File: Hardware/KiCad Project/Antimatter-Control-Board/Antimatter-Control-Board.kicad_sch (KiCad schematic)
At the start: 6 parts, among them J1 3P JST XH, SW1 SW_SPST, U1 STM32C011F6Ux, U2 AP2210N-3.3TRG1

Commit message: Copy transceiver circuit from datasheet
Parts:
- C1, C2: value C -> 10u
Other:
- added sheet Transceiver (Transceiver.kicad_sch)
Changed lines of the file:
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@@
 			)
 		)
-		(property "Value" "C"
+		(property "Value" "10u"
 			(at 93.98 92.7099 0)
 			(effects
@@
 			)
 		)
-		(property "Value" "C"
+		(property "Value" "10u"
 			(at 82.55 102.8699 0)
 			(effects
@@
 				)
 			)
+		)
+	)
+	(sheet
+		(at 218.694 32.004)
+		(size 41.402 38.354)
+		(exclude_from_sim no)
+		(in_bom yes)
+		(on_board yes)
+		(dnp no)
+		(fields_autoplaced yes)
+		(stroke
+			(width 0.1524)
+			(type solid)
+		)
+		(fill
+			(color 0 0 0 0.0000)
+		)
+		(property "Sheetname" "Transceiver"
+			(at 218.694 31.2924 0)
+			(effects
+				(font
+					(size 1.27 1.27)
+				)
+				(justify left bottom)
+			)
+		)
+		(property "Sheetfile" "Transceiver.kicad_sch"
+			(at 218.694 70.9426 0)
+			(effects
+				(font
+					(size 1.27 1.27)
+				)
+				(justify left top)
+			)
+		)
+		(instances
+			(project "Antimatter-Control-Board"
+				(path "/ab2a7697-0e5e-4b53-bb59-6796636b3acd"
+					(page "2")
+				)
+			)

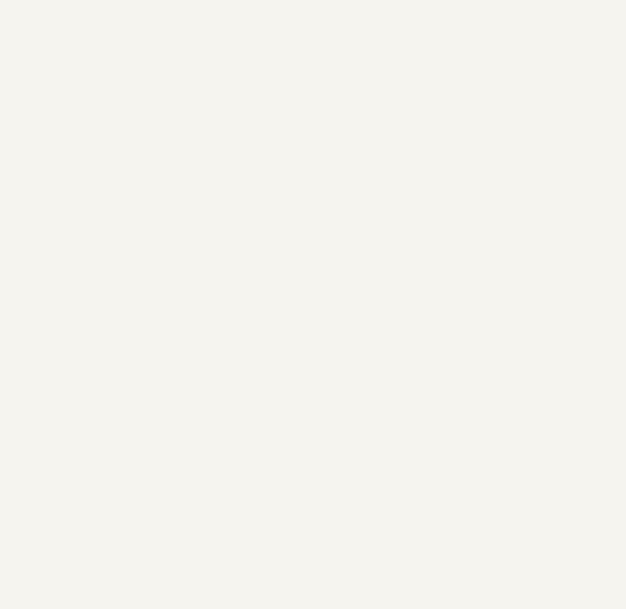
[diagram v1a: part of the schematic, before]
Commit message: Add motor driver
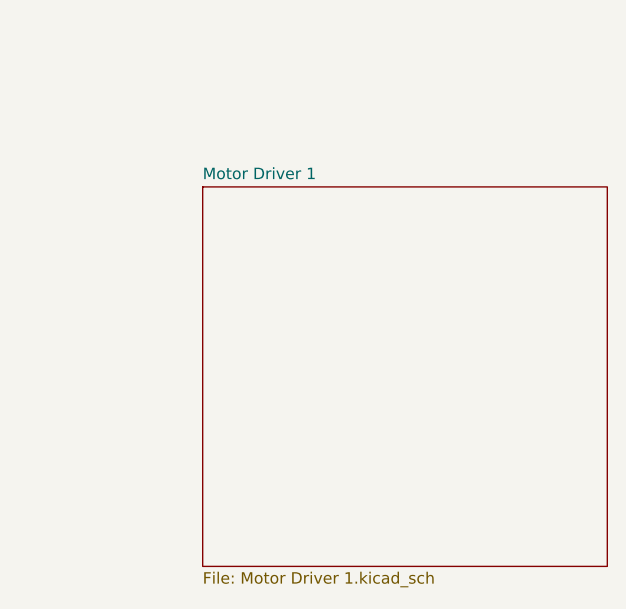
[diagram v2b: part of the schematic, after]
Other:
- added sheet Motor Driver 1 (Motor Driver 1.kicad_sch)
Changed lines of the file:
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@@
+		)
+	)
+	(sheet
+		(at 217.17 104.648)
+		(size 44.958 42.164)
+		(exclude_from_sim no)
+		(in_bom yes)
+		(on_board yes)
+		(dnp no)
+		(fields_autoplaced yes)
+		(stroke
+			(width 0.1524)
+			(type solid)
+		)
+		(fill
+			(color 0 0 0 0.0000)
+		)
+		(property "Sheetname" "Motor Driver 1"
+			(at 217.17 103.9364 0)
+			(effects
+				(font
+					(size 1.27 1.27)
+				)
+				(justify left bottom)
+			)
+		)
+		(property "Sheetfile" "Motor Driver 1.kicad_sch"
+			(at 217.17 147.3966 0)
+			(effects
+				(font
+					(size 1.27 1.27)
+				)
+				(justify left top)
+			)
+		)
+		(instances
+			(project "Antimatter-Control-Board"
+				(path "/ab2a7697-0e5e-4b53-bb59-6796636b3acd"
+					(page "3")
+				)
+			)
 		)
 	)

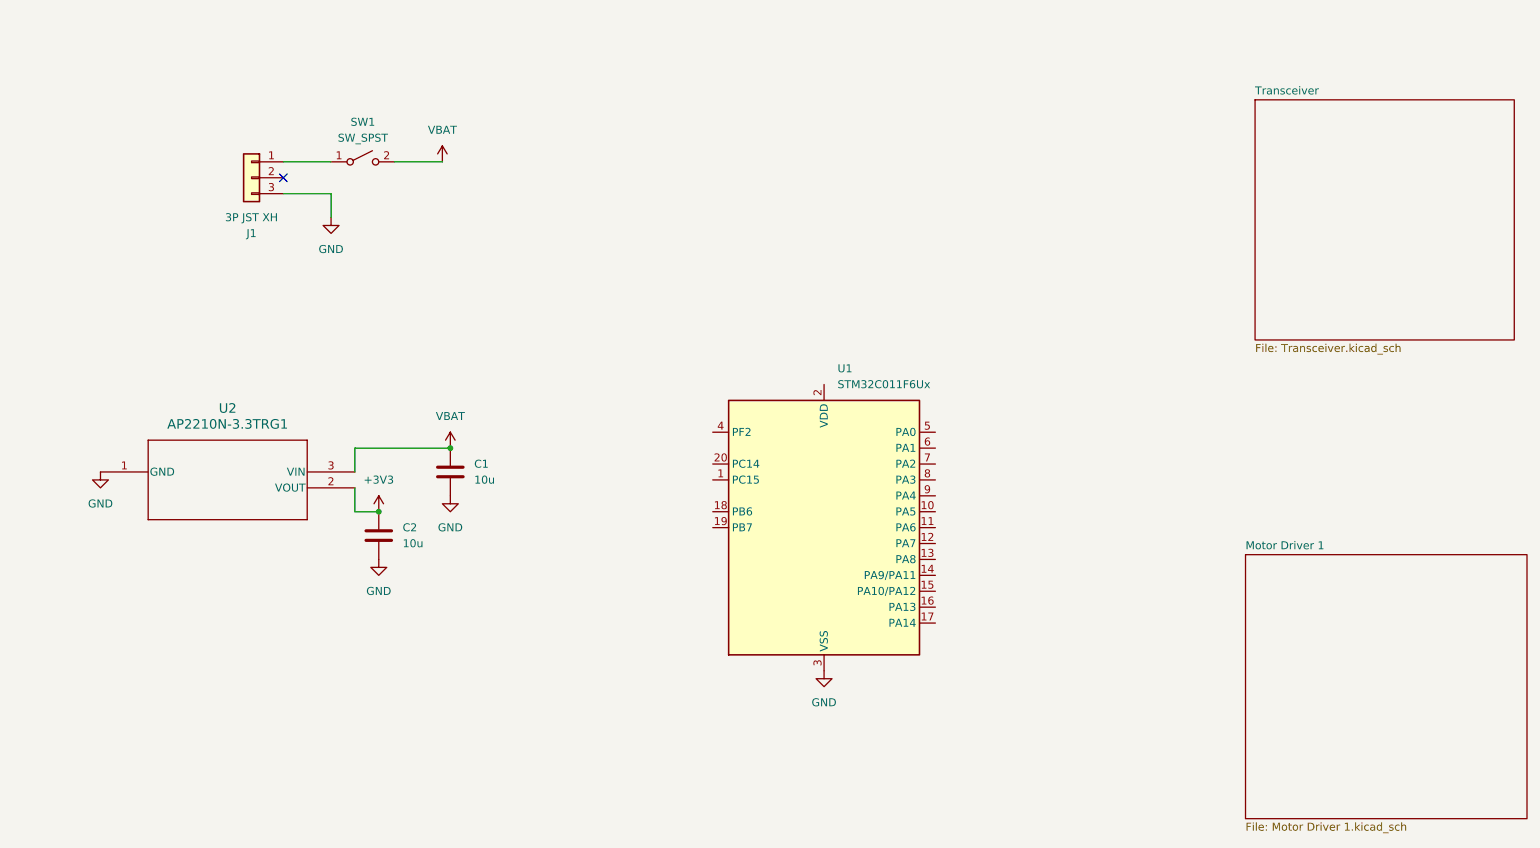
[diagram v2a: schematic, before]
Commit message: Add IMU and mag schematics
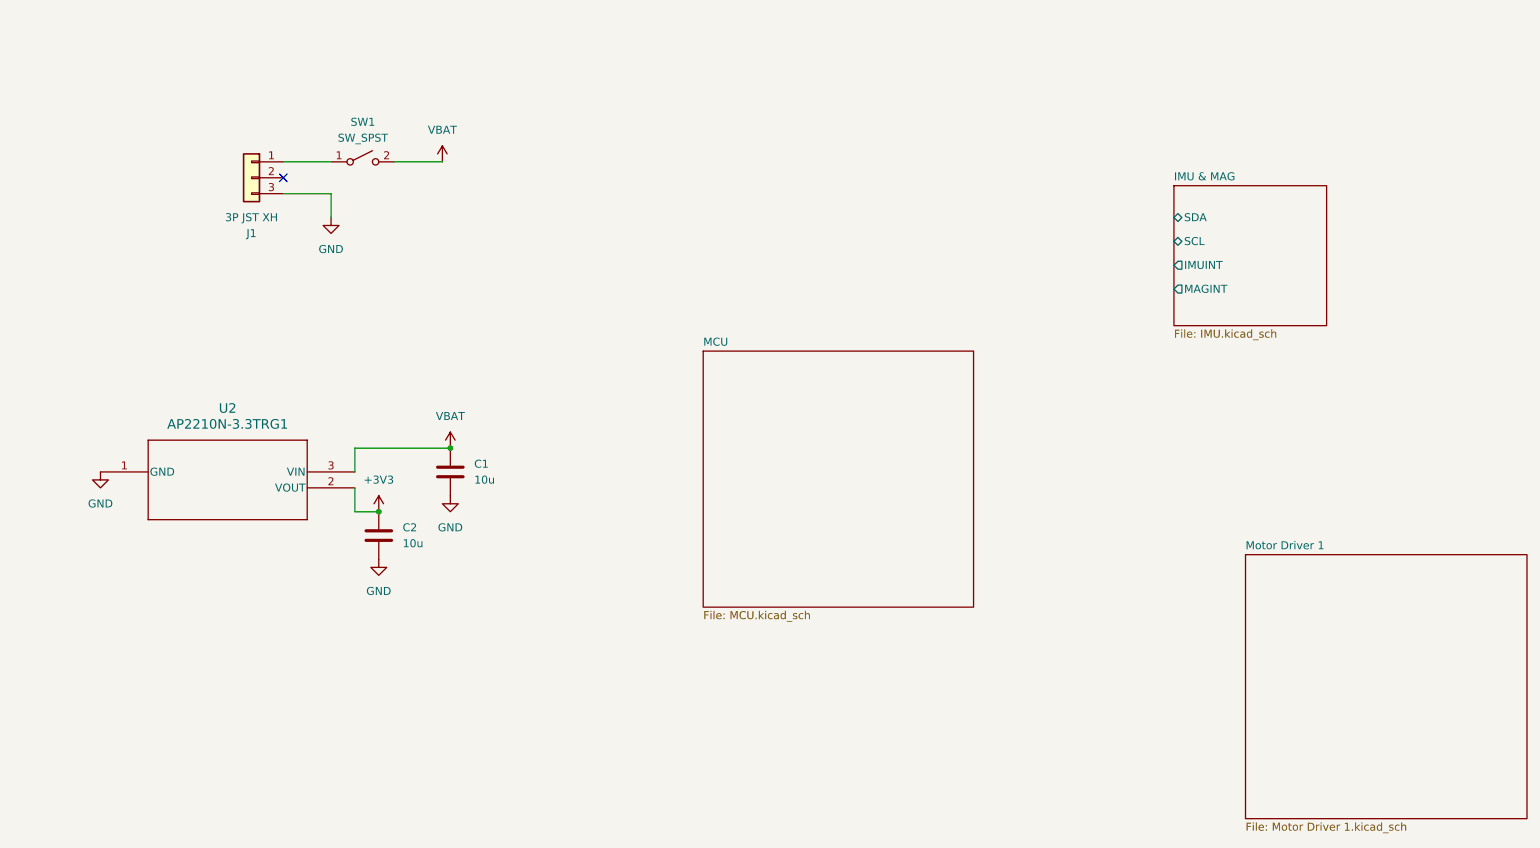
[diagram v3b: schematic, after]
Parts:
- removed U1: STM32C011F6Ux, Package_DFN_QFN:ST_UFQFPN-20_3x3mm_P0.5mm, symbol MCU_ST_STM32C0:STM32C011F6Ux
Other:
- removed sheet Transceiver
- added sheet IMU & MAG (IMU.kicad_sch)
- added sheet MCU (MCU.kicad_sch)
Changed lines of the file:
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@@
-	(symbol
-		(lib_id "power:GND")
-		(at 149.86 123.19 0)
-		(unit 1)
-		(exclude_from_sim no)
-		(in_bom yes)
-		(on_board yes)
-		(dnp no)
-		(fields_autoplaced yes)
-		(property "Reference" "#PWR01"
-			(at 149.86 129.54 0)
-			(effects
-				(font
-					(size 1.27 1.27)
-				)
-				(hide yes)
-			)
-		)
-		(property "Value" "GND"
-			(at 149.86 128.27 0)
-			(effects
-				(font
-					(size 1.27 1.27)
-				)
-			)
-		)
-		(property "Footprint" ""
-			(at 149.86 123.19 0)
-			(effects
-				(font
-					(size 1.27 1.27)
-				)
-				(hide yes)
-			)
-		)
-		(property "Datasheet" ""
-			(at 149.86 123.19 0)
-			(effects
-				(font
-					(size 1.27 1.27)
-				)
-				(hide yes)
-			)
-		)
-		(property "Description" "Power symbol creates a global label with name \"GND\" , ground"
-			(at 149.86 123.19 0)
-			(effects
-				(font
-					(size 1.27 1.27)
-				)
-				(hide yes)
-			)
-		)
-		(pin "1"
-		)
-		(instances
-			(project ""
-				(path "/ab2a7697-0e5e-4b53-bb59-6796636b3acd"
-					(reference "#PWR01")
-					(unit 1)
-				)
-			)
-		)
-	)
-	(symbol
-		(lib_id "MCU_ST_STM32C0:STM32C011F6Ux")
-		(at 149.86 100.33 0)
-		(unit 1)
-		(exclude_from_sim no)
-		(in_bom yes)
-		(on_board yes)
-		(dnp no)
-		(fields_autoplaced yes)
-		(property "Reference" "U1"
-			(at 152.0033 74.93 0)
-			(effects
-				(font
-					(size 1.27 1.27)
-				)
-				(justify left)
-			)
-		)
-		(property "Value" "STM32C011F6Ux"
-			(at 152.0033 77.47 0)
-			(effects
-				(font
-					(size 1.27 1.27)
-				)
-				(justify left)
-			)
-		)
-		(property "Footprint" "Package_DFN_QFN:ST_UFQFPN-20_3x3mm_P0.5mm"
-			(at 134.62 120.65 0)
-			(effects
-				(font
-					(size 1.27 1.27)
-				)
-				(justify right)
-				(hide yes)
-			)
-		)
-		(property "Datasheet" "https://www.st.com/resource/en/datasheet/stm32c011f6.pdf"
-			(at 149.86 100.33 0)
-			(effects
-				(font
-					(size 1.27 1.27)
-				)
-				(hide yes)
-			)
-		)
-		(property "Description" "STMicroelectronics Arm Cortex-M0+ MCU, 32KB flash, 6KB RAM, 48 MHz, 2.0-3.6V, 18 GPIO, UFQFPN20"
-			(at 149.86 100.33 0)
-			(effects
-				(font
-					(size 1.27 1.27)
-				)
-				(hide yes)
-			)
-		)
-		(pin "3"
-		)
-		(pin "4"
-		)
-		(pin "2"
-		)
-		(pin "18"
-		)
-		(pin "5"
-		)
-		(pin "13"
-		)
-		(pin "15"
-		)
-		(pin "11"
-		)
-		(pin "10"
-		)
-		(pin "17"
-		)
-		(pin "19"
-		)
-		(pin "16"
-		)
-		(pin "20"
-		)
-		(pin "7"
-		)
-		(pin "1"
-		)
-		(pin "9"
-		)
-		(pin "6"
-		)
-		(pin "12"
-		)
-		(pin "14"
-		)
-		(pin "8"
-		)
-		(instances
-			(project ""
-				(path "/ab2a7697-0e5e-4b53-bb59-6796636b3acd"
-					(reference "U1")
-					(unit 1)
-				)
-			)
-		)
-	)
 	(symbol
 		(lib_id "power:GND")
@@
 	)
 	(sheet
-		(at 218.694 32.004)
-		(size 41.402 38.354)
+		(at 205.74 45.72)
+		(size 24.384 22.352)
 		(exclude_from_sim no)
 		(in_bom yes)
@@
 			(color 0 0 0 0.0000)
 		)
-		(property "Sheetname" "Transceiver"
-			(at 218.694 31.2924 0)
+		(property "Sheetname" "IMU & MAG"
+			(at 205.74 45.0084 0)
 			(effects
 				(font
@@
 			)
 		)
-		(property "Sheetfile" "Transceiver.kicad_sch"
-			(at 218.694 70.9426 0)
+		(property "Sheetfile" "IMU.kicad_sch"
+			(at 205.74 68.6566 0)
 			(effects
 				(font
@@
 			)
 		)
+		(pin "MAGINT" output
+			(at 205.74 62.23 180)
+			(effects
+				(font
+					(size 1.27 1.27)
+				)
+				(justify left)
+			)
+		)
+		(pin "IMUINT" output
+			(at 205.74 58.42 180)
+			(effects
+				(font
+					(size 1.27 1.27)
+				)
+				(justify left)
+			)
+		)
+		(pin "SDA" bidirectional
+			(at 205.74 50.8 180)
+			(effects
+				(font
+					(size 1.27 1.27)
+				)
+				(justify left)
+			)
+		)
+		(pin "SCL" bidirectional
+			(at 205.74 54.61 180)
+			(effects
+				(font
+					(size 1.27 1.27)
+				)
+				(justify left)
+			)
+		)
 		(instances
 			(project "Antimatter-Control-Board"
 				(path "/ab2a7697-0e5e-4b53-bb59-6796636b3acd"
-					(page "2")
-				)
-			)
+					(page "4")
+				)
+			)
+		)
+	)
+	(sheet
+		(at 130.556 72.136)
+		(size 43.18 40.894)
+		(exclude_from_sim no)
+		(in_bom yes)
+		(on_board yes)
+		(dnp no)
+		(fields_autoplaced yes)
+		(stroke
+			(width 0.1524)
+			(type solid)
+		)
+		(fill
+			(color 0 0 0 0.0000)
+		)
+		(property "Sheetname" "MCU"
+			(at 130.556 71.4244 0)
+			(effects
+				(font
+					(size 1.27 1.27)
+				)
+				(justify left bottom)
+			)
+		)
+		(property "Sheetfile" "MCU.kicad_sch"
+			(at 130.556 113.6146 0)
+			(effects
+				(font
+					(size 1.27 1.27)
+				)
+				(justify left top)
+			)
+		)
+		(instances
+			(project "Antimatter-Control-Board"
+				(path "/ab2a7697-0e5e-4b53-bb59-6796636b3acd"
+					(page "3")
+				)
+			)

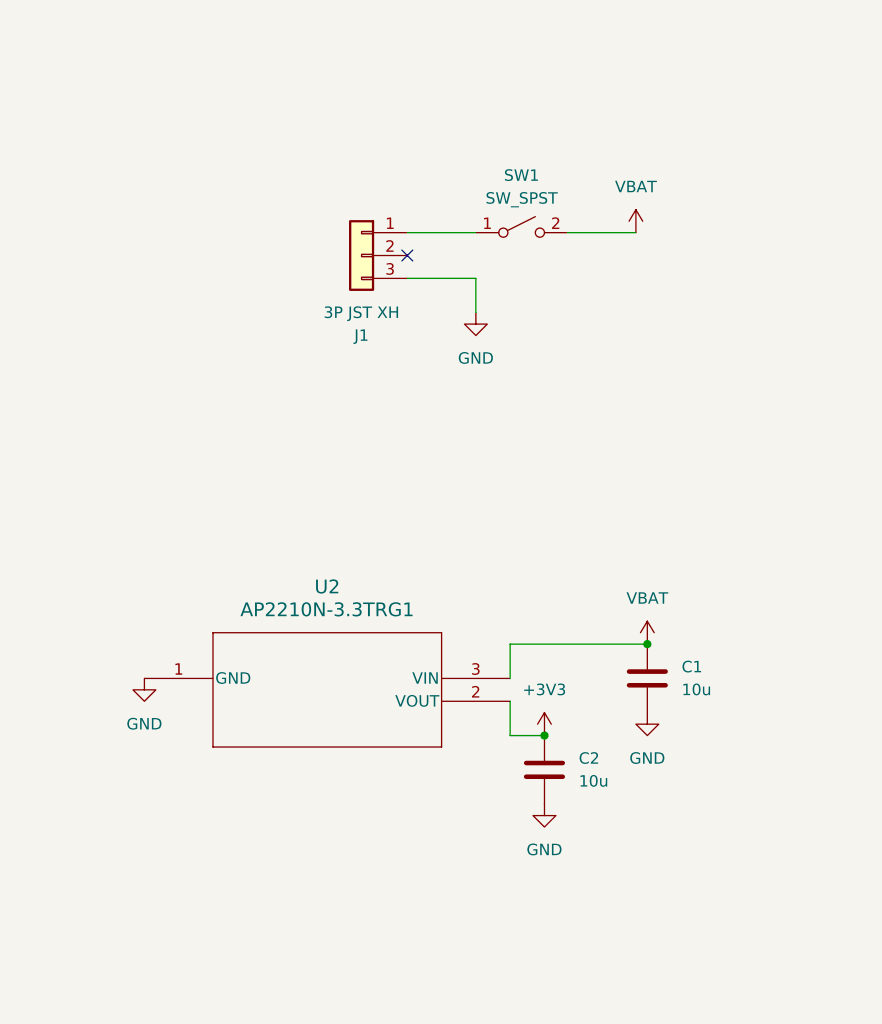
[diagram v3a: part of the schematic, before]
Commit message: Add power sheet and fix some ERC issues
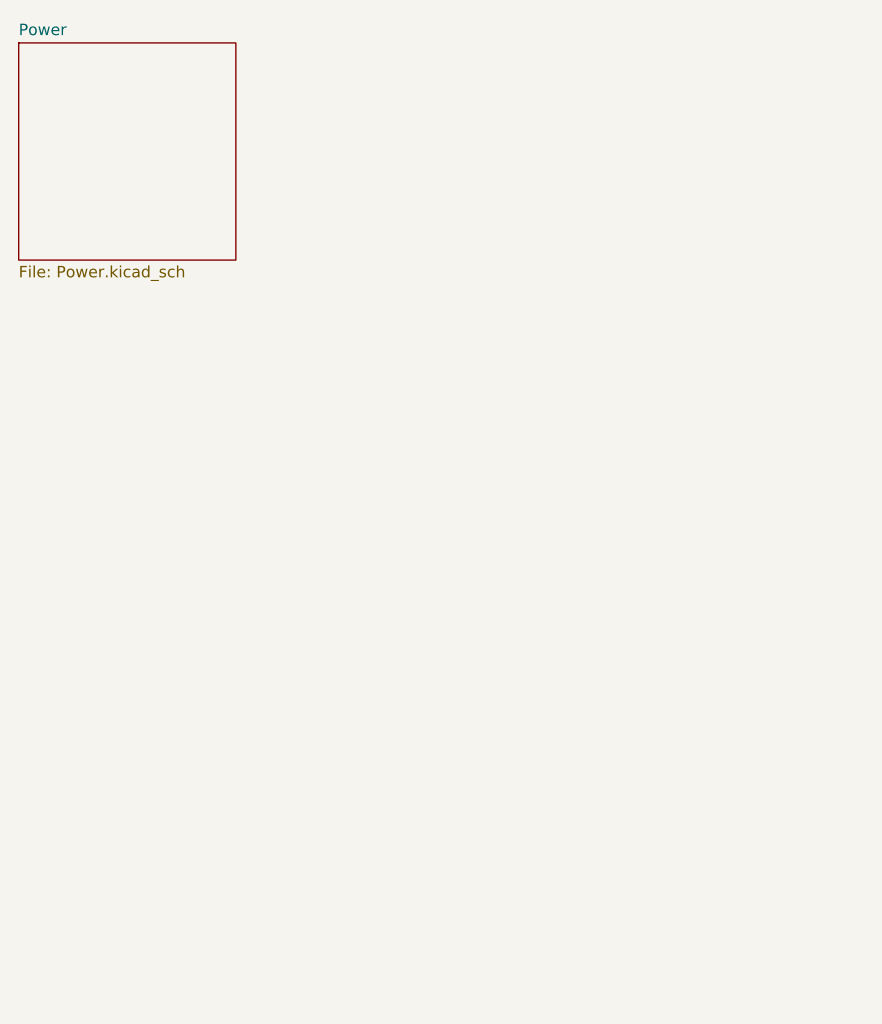
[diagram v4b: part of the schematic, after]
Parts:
- removed C1, C2: 10u, symbol Device:C
- removed J1: 3P JST XH, symbol Connector_Generic:Conn_01x03
- removed SW1: SW_SPST, symbol Switch:SW_SPST
- removed U2: AP2210N-3.3TRG1, SOT_3.3TRG1_DIO, symbol 1M_LDO:AP2210N-3.3TRG1
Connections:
- no-connect marks 1 -> 0
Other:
- added sheet Power (Power.kicad_sch)

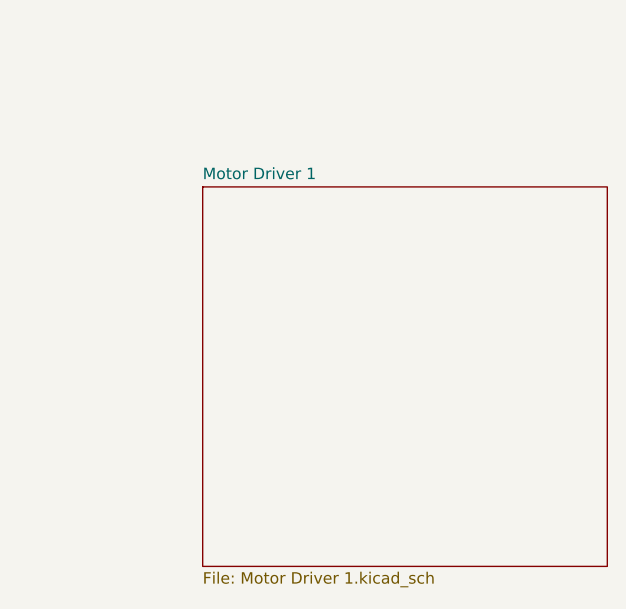
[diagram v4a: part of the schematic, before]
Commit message: Update motor driver sheet
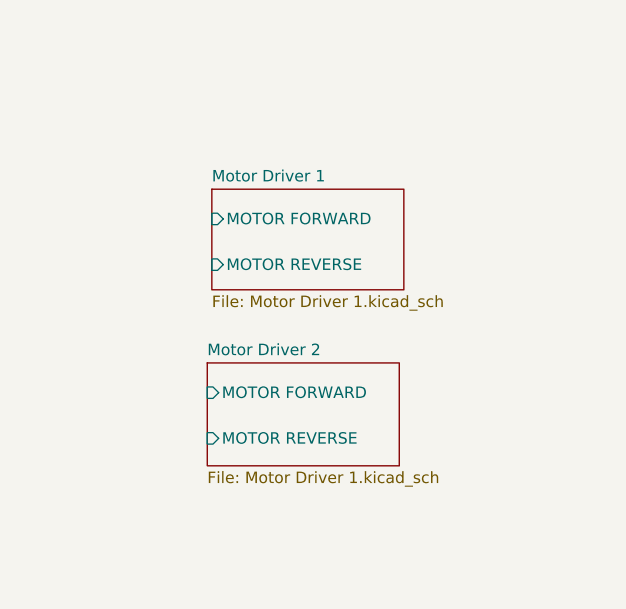
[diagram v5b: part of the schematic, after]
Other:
- added sheet Motor Driver 2 (Motor Driver 1.kicad_sch)
- sheet Motor Driver 1 ports: added MOTOR FORWARD, MOTOR REVERSE; removed none
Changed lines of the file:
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@@
 			(project "Antimatter-Control-Board"
 				(path "/ab2a7697-0e5e-4b53-bb59-6796636b3acd"
-					(page "4")
+					(page "6")
+				)
+			)
+		)
+	)
+	(sheet
+		(at 217.678 124.206)
+		(size 21.336 11.43)
+		(exclude_from_sim no)
+		(in_bom yes)
+		(on_board yes)
+		(dnp no)
+		(fields_autoplaced yes)
+		(stroke
+			(width 0.1524)
+			(type solid)
+		)
+		(fill
+			(color 0 0 0 0.0000)
+		)
+		(property "Sheetname" "Motor Driver 2"
+			(at 217.678 123.4944 0)
+			(effects
+				(font
+					(size 1.27 1.27)
+				)
+				(justify left bottom)
+			)
+		)
+		(property "Sheetfile" "Motor Driver 1.kicad_sch"
+			(at 217.678 136.2206 0)
+			(effects
+				(font
+					(size 1.27 1.27)
+				)
+				(justify left top)
+			)
+		)
+		(pin "MOTOR REVERSE" input
+			(at 217.678 132.588 180)
+			(effects
+				(font
+					(size 1.27 1.27)
+				)
+				(justify left)
+			)
+		)
+		(pin "MOTOR FORWARD" input
+			(at 217.678 127.508 180)
+			(effects
+				(font
+					(size 1.27 1.27)
+				)
+				(justify left)
+			)
+		)
+		(instances
+			(project "Antimatter-Control-Board"
+				(path "/ab2a7697-0e5e-4b53-bb59-6796636b3acd"
+					(page "5")
 				)
 			)
@@
 	)
 	(sheet
-		(at 217.17 104.648)
-		(size 44.958 42.164)
+		(at 218.186 104.902)
+		(size 21.336 11.176)
 		(exclude_from_sim no)
 		(in_bom yes)
@@
 		)
 		(property "Sheetname" "Motor Driver 1"
-			(at 217.17 103.9364 0)
+			(at 218.186 104.1904 0)
 			(effects
 				(font
@@
 		)
 		(property "Sheetfile" "Motor Driver 1.kicad_sch"
-			(at 217.17 147.3966 0)
-			(effects
-				(font
-					(size 1.27 1.27)
-				)
-				(justify left top)
-			)
-		)
-		(instances
-			(project "Antimatter-Control-Board"
-				(path "/ab2a7697-0e5e-4b53-bb59-6796636b3acd"
-					(page "3")
+			(at 218.186 116.6626 0)
+			(effects
+				(font
+					(size 1.27 1.27)
+				)
+				(justify left top)
+			)
+		)
+		(pin "MOTOR REVERSE" input
+			(at 218.186 113.284 180)
+			(effects
+				(font
+					(size 1.27 1.27)
+				)
+				(justify left)
+			)
+		)
+		(pin "MOTOR FORWARD" input
+			(at 218.186 108.204 180)
+			(effects
+				(font
+					(size 1.27 1.27)
+				)
+				(justify left)
+			)
+		)
+		(instances
+			(project "Antimatter-Control-Board"
+				(path "/ab2a7697-0e5e-4b53-bb59-6796636b3acd"
+					(page "4")
 				)
 			)
@@
 			(project "Antimatter-Control-Board"
 				(path "/ab2a7697-0e5e-4b53-bb59-6796636b3acd"
-					(page "5")
-				)
-			)
+					(page "2")
+				)
+			)
